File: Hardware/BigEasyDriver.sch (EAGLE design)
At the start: 55 parts, among them IC1 A4983ALT1, IC2 LM317L

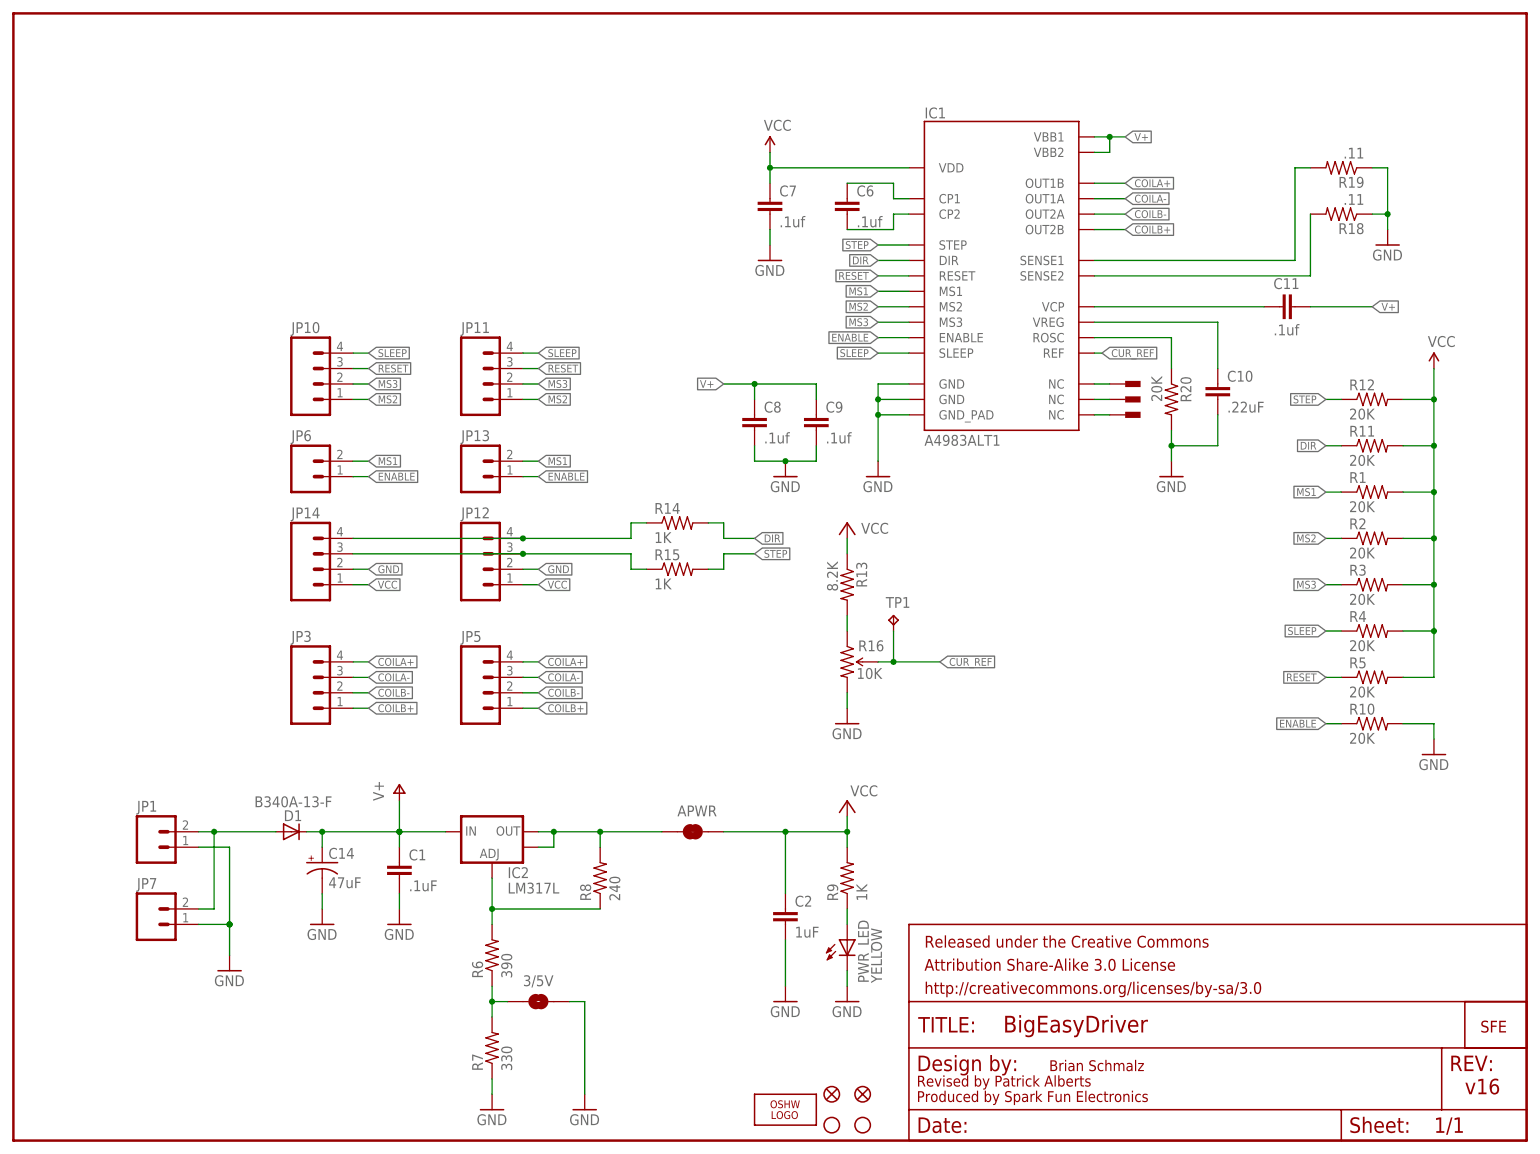
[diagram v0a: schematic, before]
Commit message: Revert "Version 1.6 update -"
This reverts commit 1063980bfb8b78f8e4fa00b59bbbd0f6b30be38e.
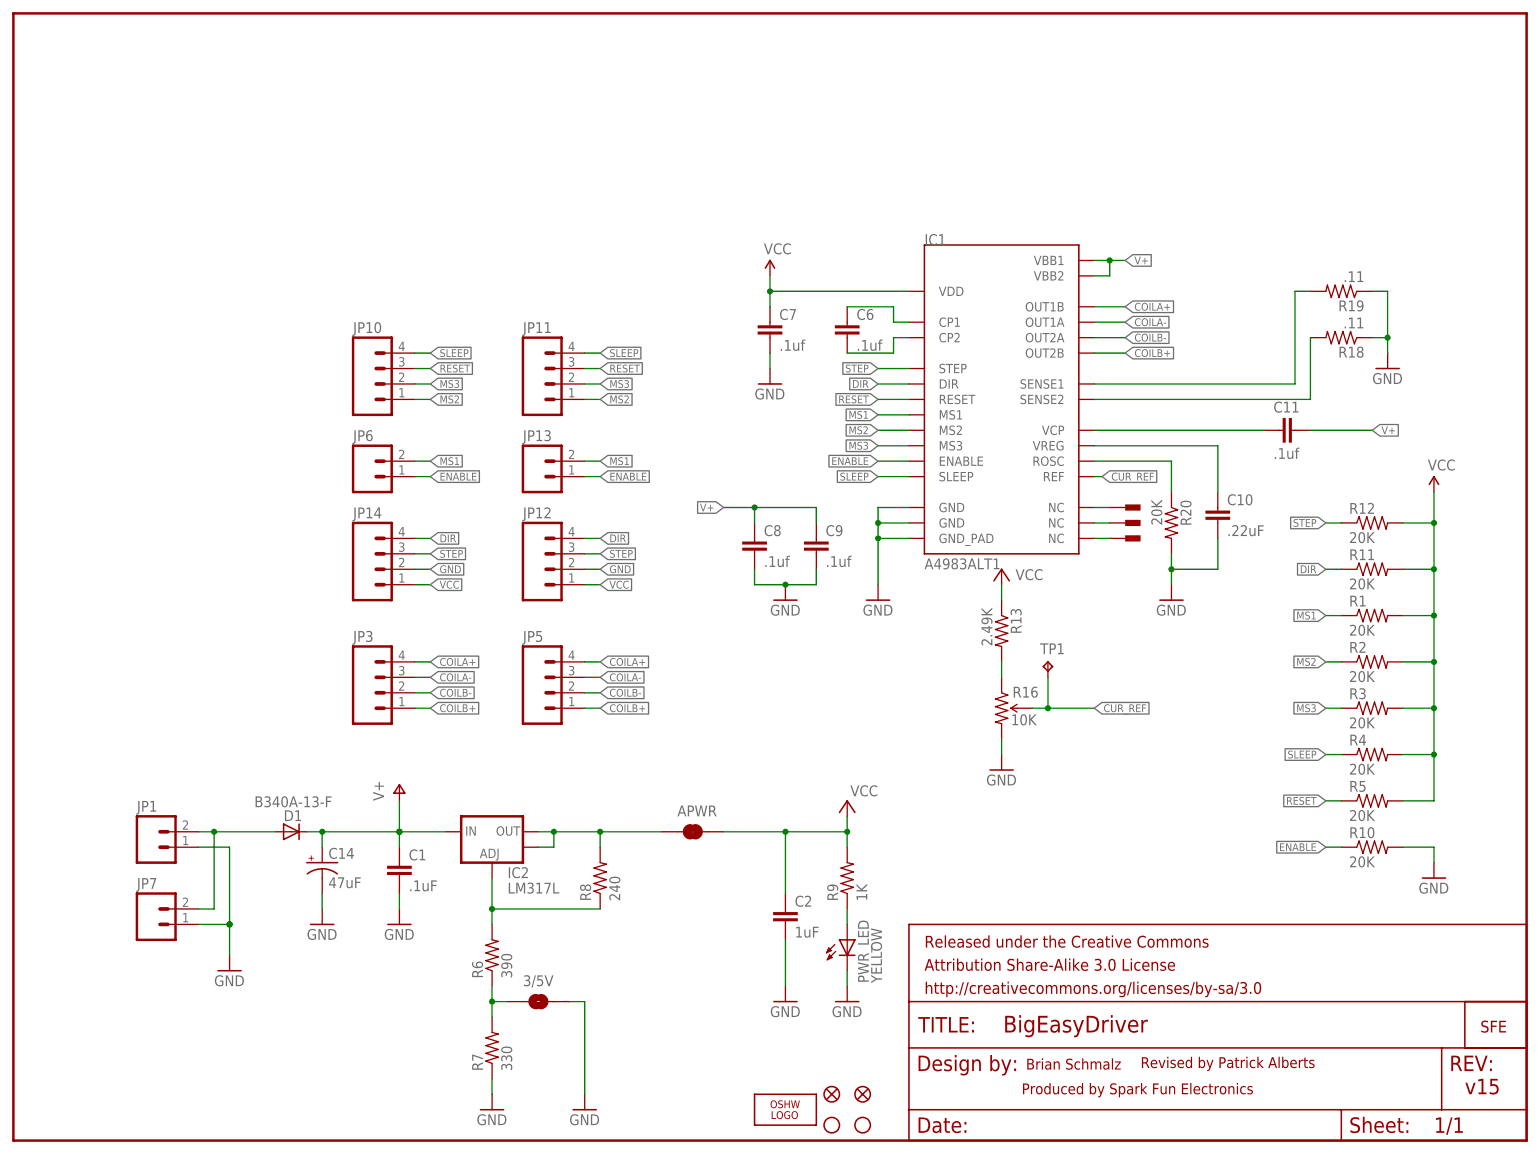
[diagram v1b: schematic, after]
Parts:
- removed R14, R15: 1K, SparkFun:RESISTOR0603-RES
- R13: value 8.2K -> 2.49K
- R16: device SparkFun-Electromechanical:TRIMPOT3MM-2 -> SparkFun:TRIMPOTSMD
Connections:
- removed net N$55: JP12.4, JP14.4, R14.1
- removed net N$56: JP12.3, JP14.3, R15.1
- net DIR: now also JP12.4, JP14.4; no longer R14.2
- net STEP: now also JP12.3, JP14.3; no longer R15.2
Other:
- note added: "1/10/12 -v13- Changes:"
- note added: "All other I/O is set to default"
- note added: "Attribution 3.0 US License"
- note added: "BigEasyDriver v1.2"
- note added: "BigEasyDriver v1.2 by Brian Schmalz is"
- note added: "Current adj pot"
- note added: "Motor current 0mA to 2.4A"
- note added: "STEP, DIR and the motor outputs"
- note added: "SparkFun design rules applied - minor layout tweaks, R13 now XXX"
- note added: "You only need to connect M+, GND"
- note added: "licensed under a Creative Commons"
- note added: "to 1/16th microstep mode"
- note added: "v1.0 Origonal version"
- note added: "v1.1 Added pull-ups, re-routed"
- note added: "v1.2 5/2/11 Silk screen corrections, sense resistors now .11 ohms"
- note added: "v15"
- note removed: "Added current limiting resistors to STEP and DIR"
- note removed: "BigEasyDriver v1.6"
- note removed: "Changed R13 to 8.2K to improve range of current adjust pot"
- note removed: "Changed license from CC by 3.0 to CC by-sa 3.0"
- note removed: "Current adjust pot: adjusts max coil current. R13 set such that: At VCC = 3.3V, full clockwise = 2.08A coil current At VCC = 5V, 64% clockwise = 2.0A coil current Note driver can only output 2A coil current, and is dependent on input voltage, motor, and heat sinking/fan to reach this."
- note removed: "Removed large hole in solder mask on bottom"
- note removed: "SparkFun design rules applied - minor layout tweaks, R13 now 2.49K"
- note removed: "Updated to standard 0603 foorprints, some rerouting, schematic nets changed"
- note removed: "You only need to connect M+, GND, STEP, DIR and the motor outputs. All other I/O is set to default to 1/16th microstep mode, and connections are not required for basic operation."
- note removed: "v1.0 BPS Origonal version"
- note removed: "v1.1 BPS Added pull-ups, re-routed"
- note removed: "v1.2 5/2/11 BPS Silk screen corrections, sense resistors now .11 ohms"
- note removed: "v1.3 SF 1/10/12"
- note removed: "v1.4 SF 4/17/2013 Fixed current adjustment pot silk so directions are correct"
- note removed: "v1.5 SF 6/27/2013"
- note removed: "v1.6 BPS 3/28/2014"
- note removed: "v16"
- moved on the sheet: C10, C11, C6, C7, C8, C9, IC1, JP10, JP11, JP12, JP13, JP14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
